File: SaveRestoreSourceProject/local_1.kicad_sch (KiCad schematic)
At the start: 3 parts

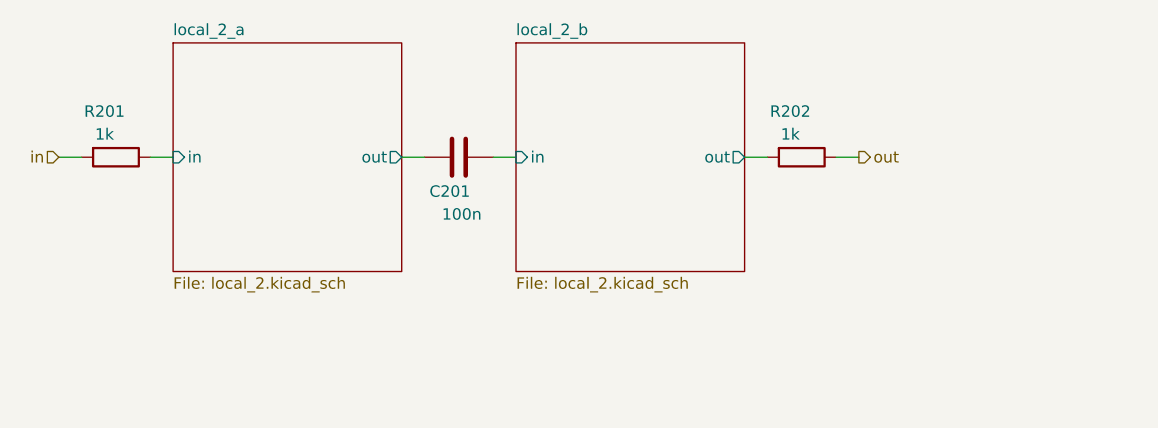
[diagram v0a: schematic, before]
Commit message: Add support for connected drawings, update test template
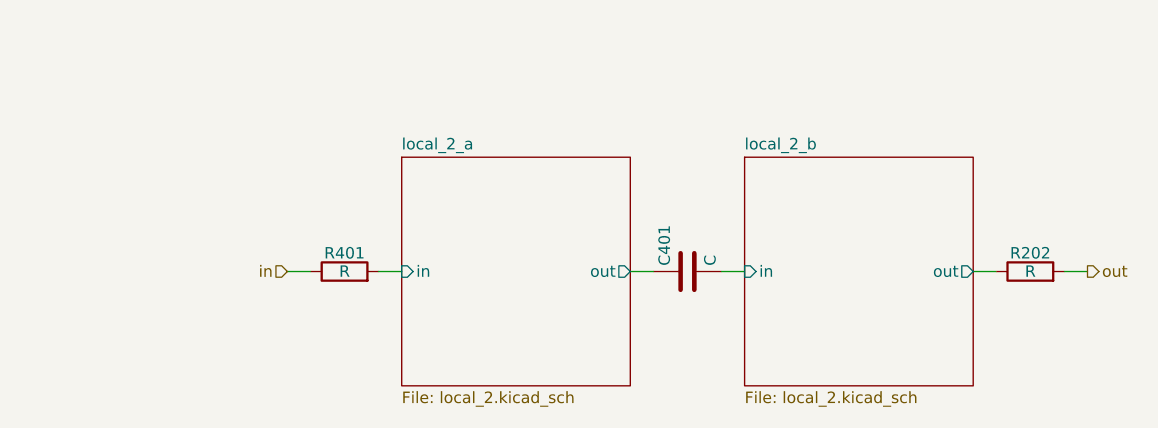
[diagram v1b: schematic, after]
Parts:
- removed C201: 100n, Capacitor_SMD:C_1206_3216Metric_Pad1.33x1.80mm_HandSolder, symbol Device:C
- removed R201: 1k, Resistor_SMD:R_1206_3216Metric, symbol Device:R
- added C401: C, Capacitor_SMD:C_1206_3216Metric, symbol Device:C
- added R401: R, Resistor_SMD:R_1206_3216Metric, symbol Device:R
- R202: value 1k -> R
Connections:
- net in: now also R401.1
- net local_2_a/in: now also R401.2
- net local_2_a/out: now also C401.1
- net local_2_b/in: now also C401.2
- net local_2_b/out: now also R202.1; no longer R202.2
- net out: now also R202.2; no longer R202.1
